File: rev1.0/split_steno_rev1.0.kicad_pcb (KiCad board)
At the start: 2 copper layers, 97.6 x 84.5 mm, 44 parts, among them J0 TRRS, K0 KEYSW, K1 KEYSW, K10 KEYSW, K11 KEYSW, K12 KEYSW, K13 KEYSW, K14 KEYSW, K15 KEYSW, K16 KEYSW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

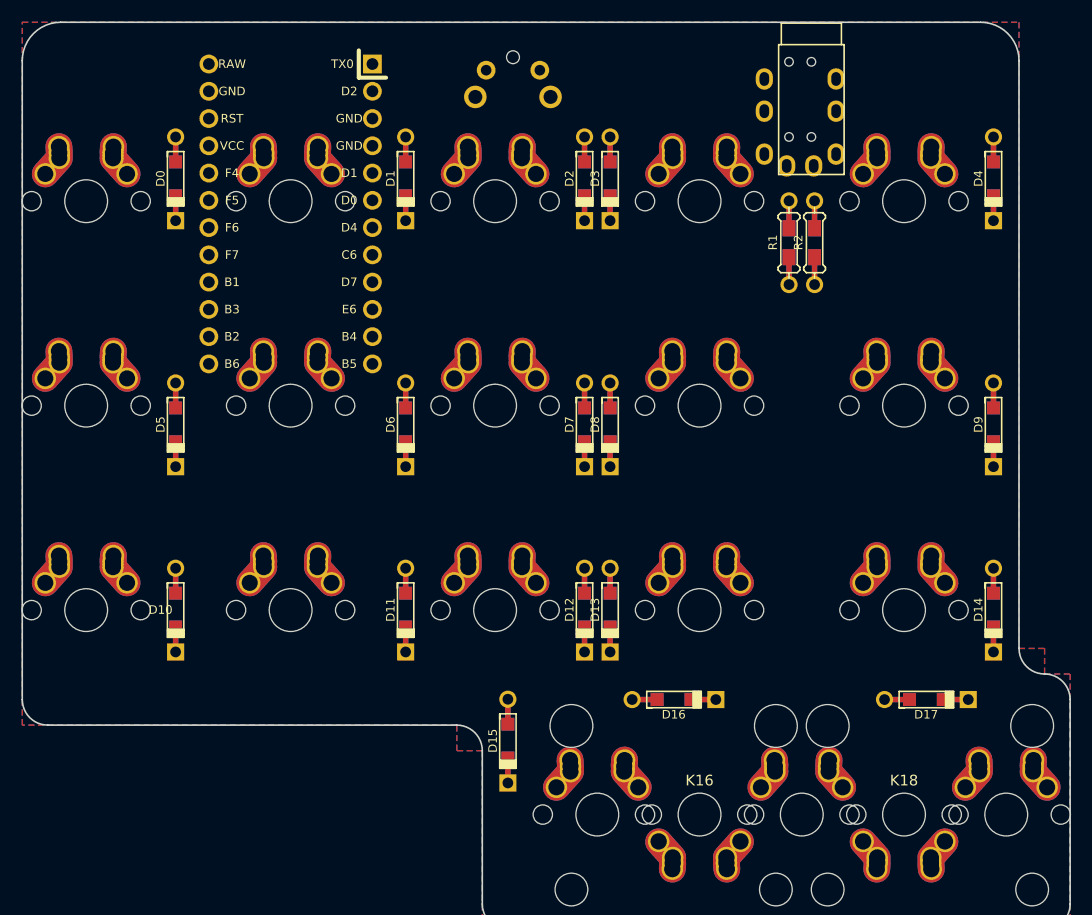
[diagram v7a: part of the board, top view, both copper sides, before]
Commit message: finished routing traces
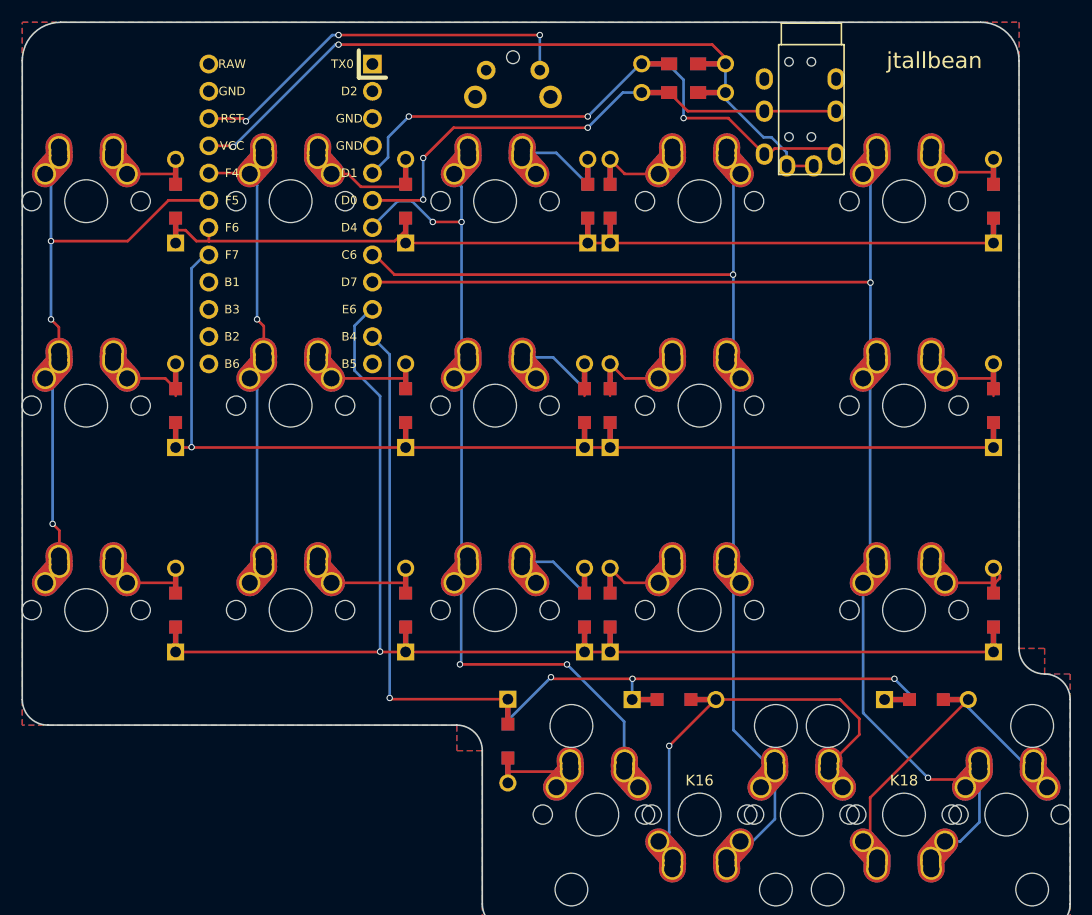
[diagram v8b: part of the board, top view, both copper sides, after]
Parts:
- removed R2: 4.7k, Keebio-Parts:Resistor-Hybrid
- added R0: 4.7k, lib_fp:Resistor-Hybrid, B.Cu at (162.8, 75.3)
- D0, D1, D10, D11, D12, D13, D14, D15, D16, D17, D2, D3, D4, D5, D6, D7, D8, D9: footprint Keebio-Parts:Diode-dual -> lib_fp:Diode-dual; moved to B.Cu
- J0: footprint Keebio-Parts:TRRS-PJ-320A -> lib_fp:TRRS-PJ-320A
- K0, K1, K10, K11, K12, K13, K14, K15, K17, K19, K2, K3, K4, K5, K6, K7, K8, K9: footprint Keebio-Parts:Hybrid_PCB_100H_Dual_hole -> lib_fp:Hybrid_PCB_100H_Dual_hole
- K16, K18: footprint Keebio-Parts:Hybrid_PCB_200H-dual-nosilk -> lib_fp:Hybrid_PCB_200H-dual-nosilk
- R1: footprint Keebio-Parts:Resistor-Hybrid -> lib_fp:Resistor-Hybrid; moved to B.Cu
- SW0: footprint Keebio-Parts:SW_Tactile_SPST_Angled_MJTP1117 -> lib_fp:SW_Tactile_SPST_Angled_MJTP1117
- U0: footprint Keebio-Parts:ArduinoProMicro -> lib_fp:ArduinoProMicro
- moved R1 17.1 mm to (162.8, 78.0), turned to 180 degrees
- moved D2 2.10 mm to (153.9, 88.1)
- moved D0 2.08 mm to (115.5, 88.1)
- moved D1 2.08 mm to (136.9, 88.1)
- moved D3 2.08 mm to (156.0, 88.1)
- moved D4 2.08 mm to (191.7, 88.1)
- moved D5 1.79 mm to (115.5, 107.2)
- moved D6 1.79 mm to (136.9, 107.2)
- moved D7 1.79 mm to (153.6, 107.2)
- moved D8 1.79 mm to (156.0, 107.2)
- moved D9 1.79 mm to (191.7, 107.2)
- turned D15 to 90 degrees
- turned D16 to 180 degrees
- turned D17 to 180 degrees
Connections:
- J0 pad 1: /d0 -> VCC
- J0 pad 2: /d1 -> /d0
- J0 pad 3: GND -> /d1
- J0 pad 4: VCC -> GND
- K13 pad 1: /c3 -> Net-(D13-Pad2)
- K13 pad 2: Net-(D13-Pad2) -> /c3
- K15 pad 1: /c2 -> Net-(D15-Pad2)
- K15 pad 2: Net-(D15-Pad2) -> /c2
- K3 pad 1: /c3 -> Net-(D3-Pad2)
- K3 pad 2: Net-(D3-Pad2) -> /c3
- K8 pad 1: /c3 -> Net-(D8-Pad2)
- K8 pad 2: Net-(D8-Pad2) -> /c3
- REF** pad 1: (no net) -> VCC
- REF** pad 2: (no net) -> /d0
- REF** pad 3: (no net) -> /d1
- REF** pad 4: (no net) -> GND
- U0 pad 10: /r1 -> /r2
- U0 pad 11: /r2 -> /r3
- U0 pad 12: /r3 -> Net-(U0-Pad12)
- U0 pad 17: /r0 -> /r1
- U0 pad 18: /c4 -> /r0
- U0 pad 19: /c3 -> /c0
- U0 pad 20: /c2 -> /c1
- U0 pad 7: Net-(U0-Pad7) -> /c2
- U0 pad 8: /c0 -> /c3
- U0 pad 9: /c1 -> /c4
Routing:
- net /c4: track 0.00 -> 120.1 mm, vias 0 -> 2
- net /r2: track 0.00 -> 120.0 mm, vias 0 -> 1
- net /c3: track 0.00 -> 102.4 mm, vias 0 -> 1
- net /r1: track 0.00 -> 99.9 mm, vias 0 -> 1
- net /r3: track 0.00 -> 90.8 mm, vias 0 -> 4
- net /c2: track 0.00 -> 86.6 mm, vias 0 -> 4
- net /r0: track 0.00 -> 80.7 mm
- net VCC: track 0.00 -> 69.4 mm, vias 0 -> 2
- net /d0: track 0.00 -> 54.1 mm, vias 0 -> 3
- net /d1: track 0.00 -> 52.8 mm, vias 0 -> 3
- net /c0: track 0.00 -> 52.0 mm, vias 0 -> 3
- net /c1: track 0.00 -> 45.6 mm, vias 0 -> 1
- net Net-(D16-Pad2): track 0.00 -> 39.9 mm, vias 0 -> 1
- net Net-(SW0-Pad1): track 0.00 -> 37.5 mm, vias 0 -> 3
- net Net-(D17-Pad2): track 0.00 -> 30.5 mm
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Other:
- board text added: "jtallbean"
- board text added: "rev1.0"
